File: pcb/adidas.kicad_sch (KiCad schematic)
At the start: 34 parts, among them J1 ISP Header, J7 Battery, J9 Shitty Add-on, U1 MPU-6050, U2 ATTINY841-SSU

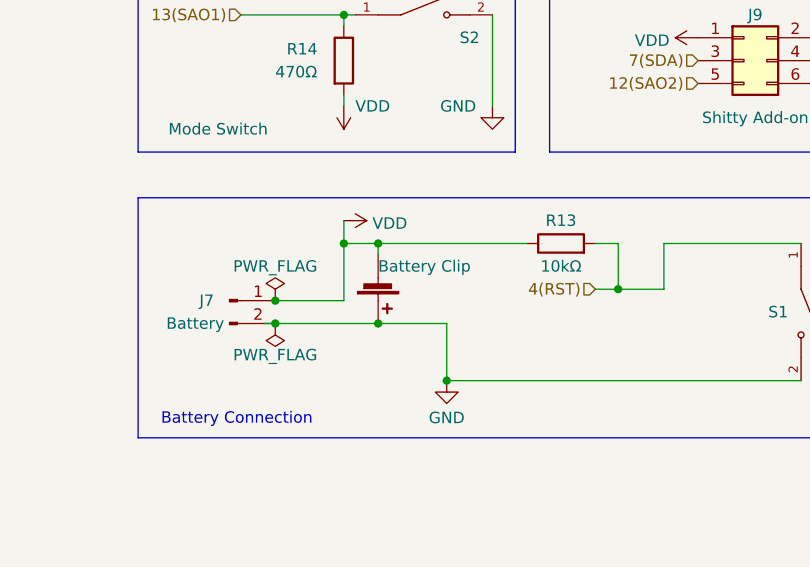
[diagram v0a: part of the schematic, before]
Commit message: fix reversed battery clip leads (#49)
* documentation updates

* documentation updates

* documentation updates

* fix battery clip
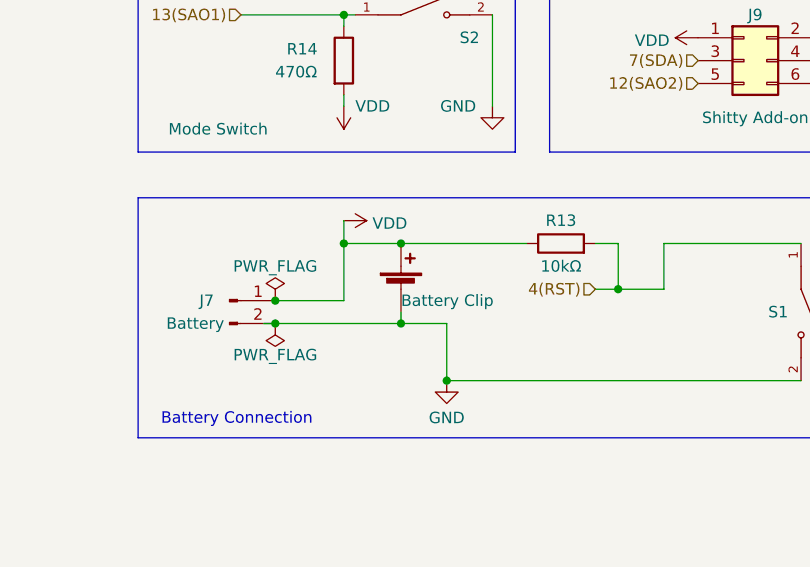
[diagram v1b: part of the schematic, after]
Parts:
- BT1: footprint Resistor_SMD:R_1206_3216Metric -> DEAD10C5:BatteryHolder_Keystone_3002_1x2032
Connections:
- net GND: now also BT1.2 (-); no longer BT1.1 (+)
- net VDD: now also BT1.1 (+); no longer BT1.2 (-)
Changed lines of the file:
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@@
     (comment 1 "Русский хардбасс")
   )
-  (junction (at 219.71 151.13) (diameter 0) (color 0 0 0 0)
-  )
   (junction (at 208.28 151.13) (diameter 0) (color 0 0 0 0)
   )
@@
   (junction (at 246.38 147.32) (diameter 0) (color 0 0 0 0)
   )
+  (junction (at 222.25 151.13) (diameter 0) (color 0 0 0 0)
+  )
   (junction (at 36.83 160.02) (diameter 0) (color 0 0 0 0)
   )
@@
   (junction (at 36.83 172.72) (diameter 0) (color 0 0 0 0)
   )
-  (junction (at 219.71 142.24) (diameter 0) (color 0 0 0 0)
-  )
   (junction (at 86.36 160.02) (diameter 0) (color 0 0 0 0)
   )
   (junction (at 111.76 160.02) (diameter 0) (color 0 0 0 0)
+  )
+  (junction (at 222.25 142.24) (diameter 0) (color 0 0 0 0)
   )
   (junction (at 168.91 160.02) (diameter 0) (color 0 0 0 0)
@@
     (stroke (width 0) (type default))
   )
-  (wire (pts (xy 219.71 151.13) (xy 227.33 151.13))
-    (stroke (width 0) (type default))
-  )
   (wire (pts (xy 215.9 116.84) (xy 217.17 116.84))
     (stroke (width 0) (type default))
   )
+  (wire (pts (xy 222.25 142.24) (xy 236.22 142.24))
+    (stroke (width 0) (type default))
+  )
   (wire (pts (xy 106.68 160.02) (xy 111.76 160.02))
     (stroke (width 0) (type default))
@@
     (stroke (width 0) (type default))
   )
-  (wire (pts (xy 219.71 142.24) (xy 236.22 142.24))
-    (stroke (width 0) (type default))
-  )
-  (wire (pts (xy 219.71 142.24) (xy 219.71 143.51))
+  (wire (pts (xy 215.9 142.24) (xy 222.25 142.24))
     (stroke (width 0) (type default))
   )
@@
     (stroke (width 0) (type default))
   )
+  (wire (pts (xy 222.25 151.13) (xy 227.33 151.13))
+    (stroke (width 0) (type default))
+  )
   (wire (pts (xy 224.79 50.8) (xy 224.79 53.34))
     (stroke (width 0) (type default))
@@
     (stroke (width 0) (type default))
   )
-  (wire (pts (xy 215.9 142.24) (xy 219.71 142.24))
-    (stroke (width 0) (type default))
-  )
   (wire (pts (xy 251.46 142.24) (xy 266.7 142.24))
     (stroke (width 0) (type default))
@@
     (stroke (width 0) (type default))
   )
-  (wire (pts (xy 208.28 151.13) (xy 219.71 151.13))
+  (wire (pts (xy 208.28 151.13) (xy 222.25 151.13))
+    (stroke (width 0) (type default))
+  )
+  (wire (pts (xy 222.25 149.86) (xy 222.25 151.13))
     (stroke (width 0) (type default))
   )
@@
     )
   )
-  (symbol (lib_id "Device:Battery_Cell") (at 219.71 146.05 0) (mirror x) (unit 1)
+  (symbol (lib_id "Device:Battery_Cell") (at 222.25 147.32 0) (unit 1)
     (in_bom no) (on_board yes) (dnp no)
-    (property "Reference" "BT1" (at 222.631 148.7257 0)
+    (property "Reference" "BT1" (at 225.171 144.6443 0)
       (effects (font (size 1.27 1.27)) (justify left) hide)
     )
-    (property "Value" "Battery Clip" (at 219.71 144.78 0)
-      (effects (font (size 1.27 1.27)) (justify left))
-    )
-    (property "Footprint" "Resistor_SMD:R_1206_3216Metric" (at 219.71 147.574 90)
-      (effects (font (size 1.27 1.27)) hide)
-    )
-    (property "Datasheet" "https://www.mouser.com/datasheet/2/215/3000TR-742873.pdf" (at 219.71 147.574 90)
-      (effects (font (size 1.27 1.27)) hide)
-    )
-    (property "Mouser Part Number`" "534-3000TR" (at 219.71 146.05 0)
-      (effects (font (size 1.27 1.27)) hide)
-    )
-    (property "Manufacturer Product Number" "3000TR" (at 219.71 146.05 0)
-      (effects (font (size 1.27 1.27)) hide)
-    )
-    (property "Manufacturer" "Keystone Electronics" (at 219.71 146.05 0)
-      (effects (font (size 1.27 1.27)) hide)
-    )
-    (property "Description" "CR2032 Coin Cell Battery Holder" (at 219.71 146.05 0)
-      (effects (font (size 1.27 1.27)) hide)
-    )
+    (property "Value" "Battery Clip" (at 222.25 148.59 0)
+      (effects (font (size 1.27 1.27)) (justify left))
+    )
+    (property "Footprint" "DEAD10C5:BatteryHolder_Keystone_3002_1x2032" (at 222.25 145.796 90)
+      (effects (font (size 1.27 1.27)) hide)
+    )
+    (property "Datasheet" "https://www.mouser.com/datasheet/2/215/3000TR-742873.pdf" (at 222.25 145.796 90)
+      (effects (font (size 1.27 1.27)) hide)
+    )
+    (property "Mouser Part Number`" "534-3000TR" (at 222.25 147.32 0)
+      (effects (font (size 1.27 1.27)) hide)
+    )
+    (property "Manufacturer Product Number" "3000TR" (at 222.25 147.32 0)
+      (effects (font (size 1.27 1.27)) hide)
+    )
+    (property "Manufacturer" "Keystone Electronics" (at 222.25 147.32 0)
+      (effects (font (size 1.27 1.27)) hide)
+    )
+    (property "Description" "CR2032 Coin Cell Battery Holder" (at 222.25 147.32 0)
+      (effects (font (size 1.27 1.27)) hide)
+    )

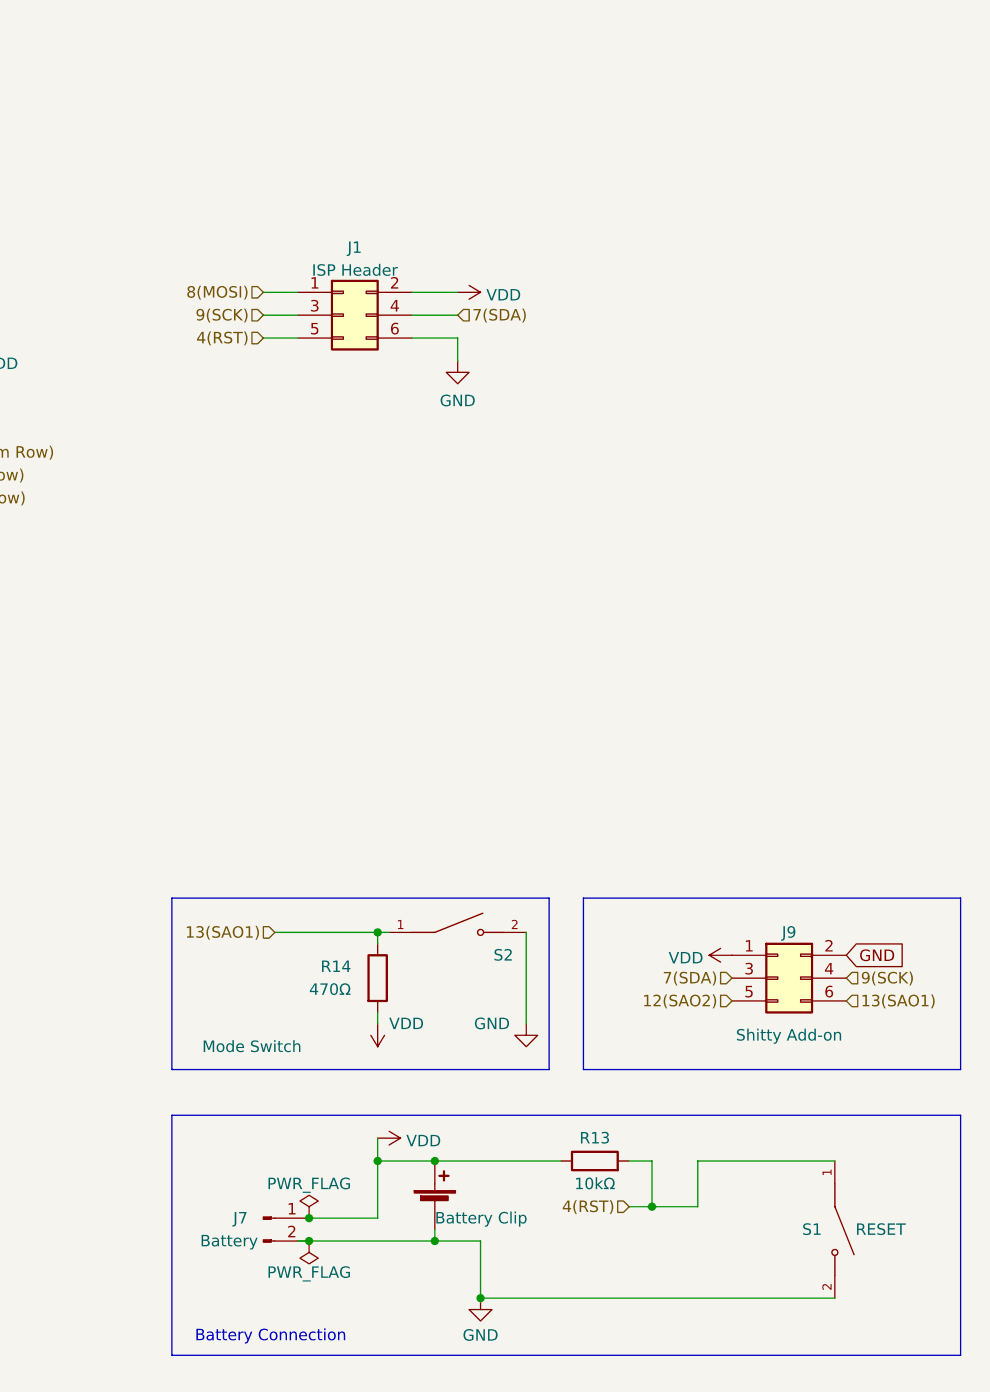
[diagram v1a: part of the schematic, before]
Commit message: hardware testing (#50)
* hardware testing

* hardware testing

* new hardware test with wire library

* add some docs on how the new test code is meant to work

* add docs for flashing the boards

* add test pin breakouts

* more testing

* checkpoint some test code

* add serial port

* testing pins

* testing pins
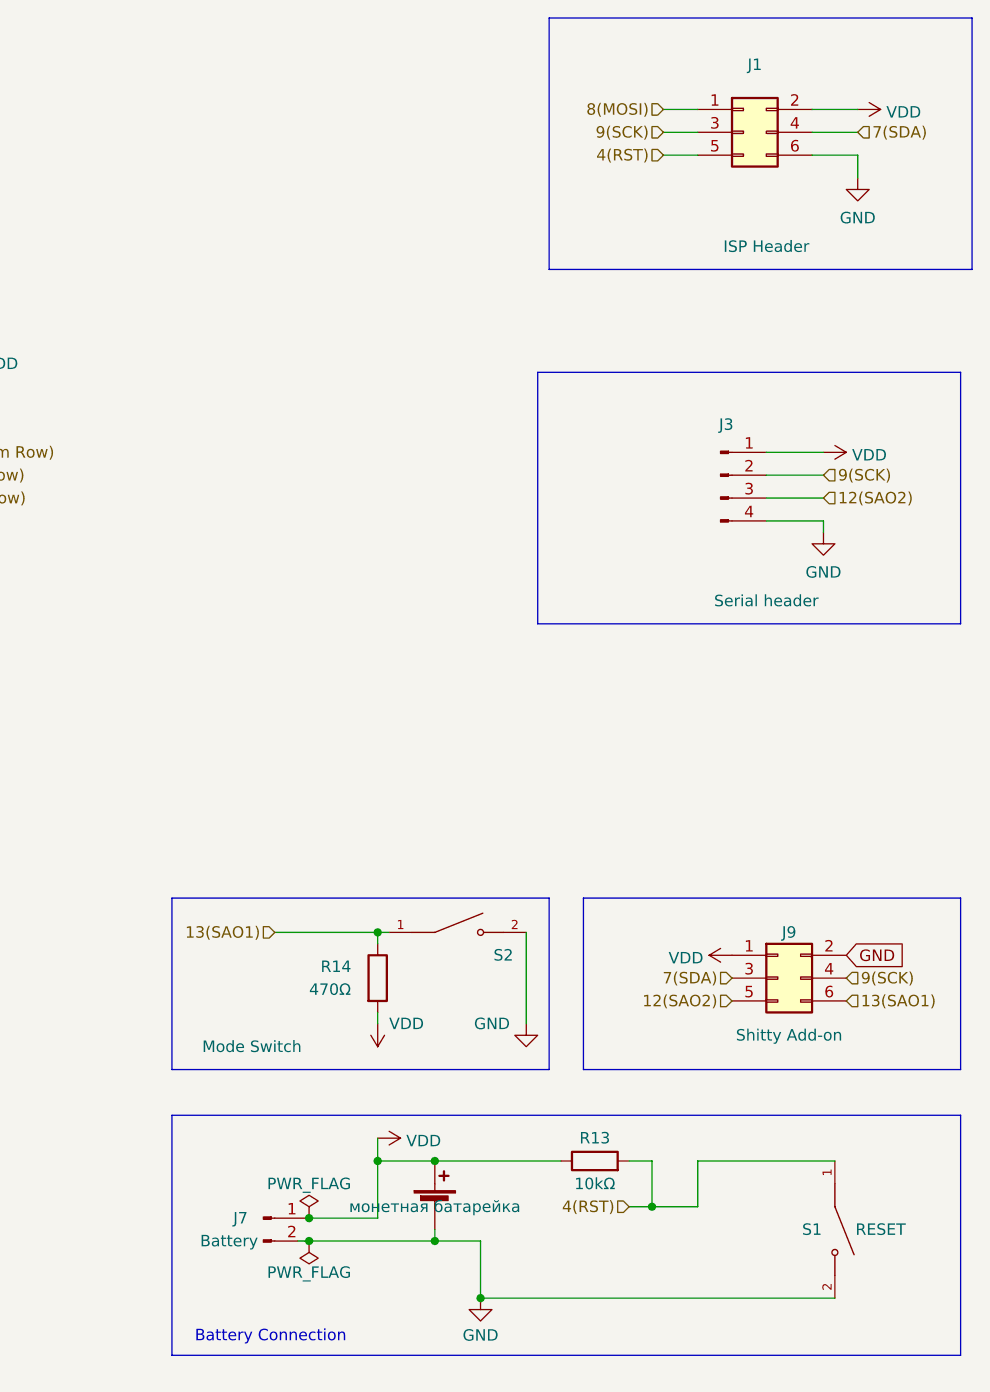
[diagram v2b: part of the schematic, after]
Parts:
- added J3: Conn_01x04_Pin, Connector_PinHeader_2.54mm:PinHeader_1x04_P2.54mm_Vertical, symbol Connector:Conn_01x04_Pin
- BT1: val (none) -> монетная батарейка
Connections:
- net 12(SAO2): now also J3.3 (Pin_3)
- net 9(SCK): now also J3.2 (Pin_2)
- net GND: now also J3.4 (Pin_4)
- net VDD: now also J3.1 (Pin_1)
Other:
- moved on the sheet: J1

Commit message: updates to the back of the board
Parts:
- BT1: value Battery Clip -> монетная батарейка
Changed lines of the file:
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@@
       (effects (font (size 1.27 1.27)) (justify left) hide)
     )
-    (property "Value" "Battery Clip" (at 222.25 148.59 0)
+    (property "Value" "монетная батарейка" (at 222.25 148.59 0)
       (effects (font (size 1.27 1.27)) (justify left) hide)
     )

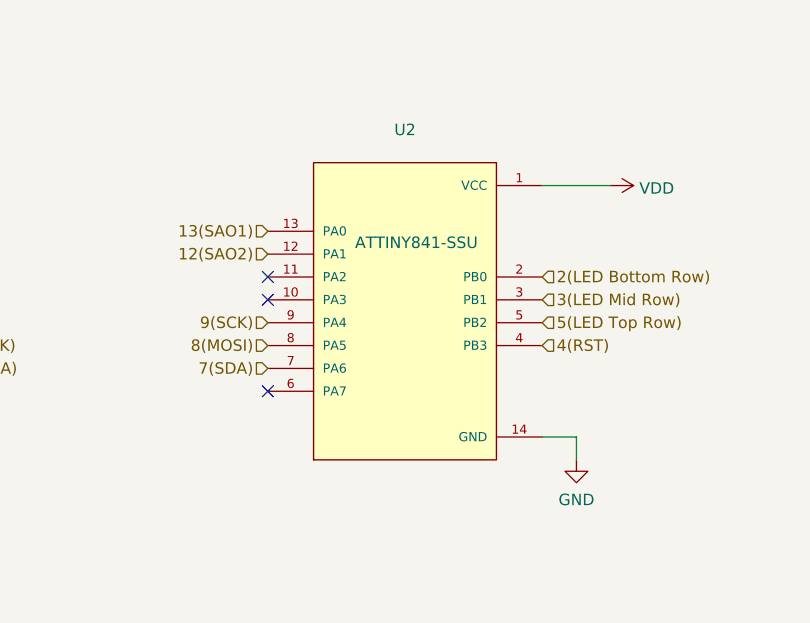
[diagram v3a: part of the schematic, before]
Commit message: flip the battery clip (#57)
* flip the battery clip

* update BOM and generate gerbers
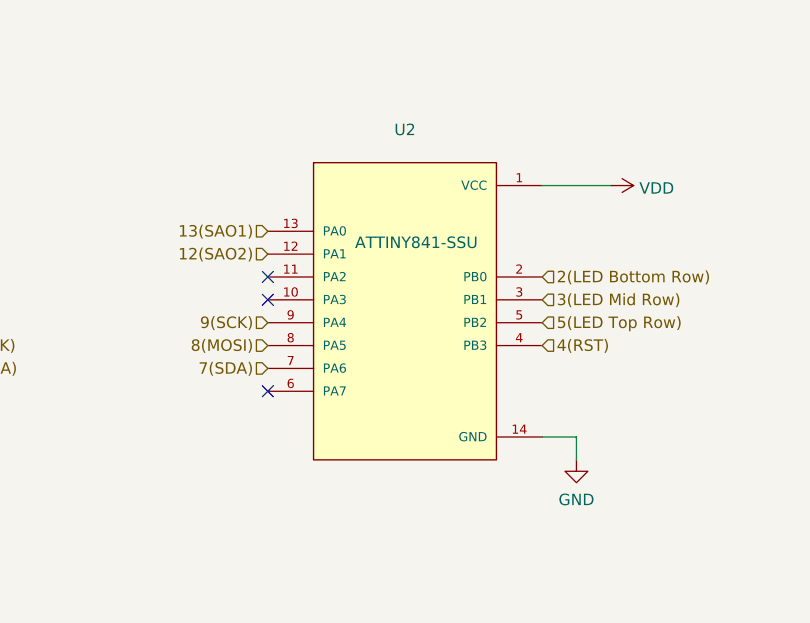
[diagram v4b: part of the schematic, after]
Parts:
- U2: A1_MIN 0.1 -> (none); A_MAX 1.75 -> (none); A_MIN 1.75 -> (none); A_NOM 1.75 -> (none); B_MAX 0.5 -> (none); B_MIN 0.33 -> (none); B_NOM 0.415 -> (none); D2_MAX 0.0 -> (none); D_MAX 8.74 -> (none); D_MIN 8.55 -> (none); D_NOM 8.645 -> (none); E1_MAX 3.99 -> (none); E1_MIN 3.8 -> (none); E1_NOM 3.895 -> (none); E2_MAX 0.0 -> (none); ENOM 1.27 -> (none); E_MAX 6.19 -> (none); E_MIN 5.8 -> (none); E_NOM 5.995 -> (none); L_MAX 1.27 -> (none); L_MIN 0.41 -> (none); L_NOM 0.84 -> (none); MANUFACTURER Microchip -> (none); MAXIMUM_PACKAGE_HEIGHT 1.75mm -> (none); Manufacturer Microchip -> (none); Mouser Part 556-ATTINY841-SSU -> (none); PACKAGE_TYPE SOIC-14 -> (none); PARTREV A -> (none); PIN_COUNT 14.0 -> (none); STANDARD IPC 7351B -> (none)
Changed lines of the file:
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@@
   (title_block
     (title "гопник badge")
-    (date "2023-05-11")
+    (date "2023-06-01")
     (rev "v0.3")
     (company "DE:AD:10:C5")
     (comment 1 "Русский хардбасс")
+    (comment 2 "DEFCON XXXI")
   )
   (junction (at 208.28 151.13) (diameter 0) (color 0 0 0 0)
@@
       (effects (font (size 1.27 1.27)) (justify left bottom) hide)
     )
-    (property "PACKAGE_TYPE" "SOIC-14" (at 146.05 66.04 0)
-      (effects (font (size 1.27 1.27)) (justify left bottom) hide)
-    )
-    (property "Manufacturer" "Microchip" (at 146.05 66.04 0)
-      (effects (font (size 1.27 1.27)) (justify left bottom) hide)
-    )
-    (property "MAXIMUM_PACKAGE_HEIGHT" "1.75mm" (at 146.05 66.04 0)
-      (effects (font (size 1.27 1.27)) (justify left bottom) hide)
-    )
-    (property "Mouser Part" "556-ATTINY841-SSU" (at 146.05 66.04 0)
-      (effects (font (size 1.27 1.27)) hide)
-    )
-    (property "B_NOM" "0.415" (at 146.05 66.04 0)
-      (effects (font (size 1.27 1.27)) (justify left bottom) hide)
-    )
-    (property "B_MIN" "0.33" (at 146.05 66.04 0)
-      (effects (font (size 1.27 1.27)) (justify left bottom) hide)
-    )
-    (property "D_MIN" "8.55" (at 146.05 66.04 0)
-      (effects (font (size 1.27 1.27)) (justify left bottom) hide)
-    )
-    (property "PINS" "" (at 146.05 66.04 0)
-      (effects (font (size 1.27 1.27)) (justify left bottom) hide)
-    )
-    (property "E2_MAX" "0.0" (at 146.05 66.04 0)
-      (effects (font (size 1.27 1.27)) (justify left bottom) hide)
-    )
-    (property "L1_MIN" "" (at 146.05 66.04 0)
-      (effects (font (size 1.27 1.27)) (justify left bottom) hide)
-    )
-    (property "D1_NOM" "" (at 146.05 66.04 0)
-      (effects (font (size 1.27 1.27)) (justify left bottom) hide)
-    )
-    (property "PARTREV" "A" (at 146.05 66.04 0)
-      (effects (font (size 1.27 1.27)) (justify left bottom) hide)
-    )
-    (property "A_NOM" "1.75" (at 146.05 66.04 0)
-      (effects (font (size 1.27 1.27)) (justify left bottom) hide)
-    )
-    (property "STANDARD" "IPC 7351B" (at 146.05 66.04 0)
-      (effects (font (size 1.27 1.27)) (justify left bottom) hide)
-    )
-    (property "D1_MIN" "" (at 146.05 66.04 0)
-      (effects (font (size 1.27 1.27)) (justify left bottom) hide)
-    )
-    (property "D_MAX" "8.74" (at 146.05 66.04 0)
-      (effects (font (size 1.27 1.27)) (justify left bottom) hide)
-    )
-    (property "L1_MAX" "" (at 146.05 66.04 0)
-      (effects (font (size 1.27 1.27)) (justify left bottom) hide)
-    )
-    (property "VACANCIES" "" (at 146.05 66.04 0)
-      (effects (font (size 1.27 1.27)) (justify left bottom) hide)
-    )
-    (property "E1_MAX" "3.99" (at 146.05 66.04 0)
-      (effects (font (size 1.27 1.27)) (justify left bottom) hide)
-    )
-    (property "DMIN" "" (at 146.05 66.04 0)
-      (effects (font (size 1.27 1.27)) (justify left bottom) hide)
-    )
-    (property "E1_MIN" "3.8" (at 146.05 66.04 0)
-      (effects (font (size 1.27 1.27)) (justify left bottom) hide)
-    )
-    (property "MANUFACTURER" "Microchip" (at 146.05 66.04 0)
-      (effects (font (size 1.27 1.27)) (justify left bottom) hide)
-    )
-    (property "L_MAX" "1.27" (at 146.05 66.04 0)
-      (effects (font (size 1.27 1.27)) (justify left bottom) hide)
-    )
-    (property "E1_NOM" "3.895" (at 146.05 66.04 0)
-      (effects (font (size 1.27 1.27)) (justify left bottom) hide)
-    )
-    (property "E_MAX" "6.19" (at 146.05 66.04 0)
-      (effects (font (size 1.27 1.27)) (justify left bottom) hide)
-    )
-    (property "D1_MAX" "" (at 146.05 66.04 0)
-      (effects (font (size 1.27 1.27)) (justify left bottom) hide)
-    )
-    (property "DMAX" "" (at 146.05 66.04 0)
-      (effects (font (size 1.27 1.27)) (justify left bottom) hide)
-    )
-    (property "E_NOM" "5.995" (at 146.05 66.04 0)
-      (effects (font (size 1.27 1.27)) (justify left bottom) hide)
-    )
-    (property "D_NOM" "8.645" (at 146.05 66.04 0)
-      (effects (font (size 1.27 1.27)) (justify left bottom) hide)
-    )
-    (property "A_MIN" "1.75" (at 146.05 66.04 0)
-      (effects (font (size 1.27 1.27)) (justify left bottom) hide)
-    )
-    (property "B_MAX" "0.5" (at 146.05 66.04 0)
-      (effects (font (size 1.27 1.27)) (justify left bottom) hide)
-    )
-    (property "ENOM" "1.27" (at 146.05 66.04 0)
-      (effects (font (size 1.27 1.27)) (justify left bottom) hide)
-    )
-    (property "D2_MAX" "0.0" (at 146.05 66.04 0)
-      (effects (font (size 1.27 1.27)) (justify left bottom) hide)
-    )
-    (property "SNAPEDA_PACKAGE_ID" "" (at 146.05 66.04 0)
-      (effects (font (size 1.27 1.27)) (justify left bottom) hide)
-    )
-    (property "L_NOM" "0.84" (at 146.05 66.04 0)
-      (effects (font (size 1.27 1.27)) (justify left bottom) hide)
-    )
-    (property "DNOM" "" (at 146.05 66.04 0)
-      (effects (font (size 1.27 1.27)) (justify left bottom) hide)
-    )
-    (property "EMIN" "" (at 146.05 66.04 0)
-      (effects (font (size 1.27 1.27)) (justify left bottom) hide)
-    )
-    (property "A_MAX" "1.75" (at 146.05 66.04 0)
-      (effects (font (size 1.27 1.27)) (justify left bottom) hide)
-    )
-    (property "PIN_COUNT" "14.0" (at 146.05 66.04 0)
-      (effects (font (size 1.27 1.27)) (justify left bottom) hide)
-    )
-    (property "EMAX" "" (at 146.05 66.04 0)
-      (effects (font (size 1.27 1.27)) (justify left bottom) hide)
-    )
-    (property "A1_MIN" "0.1" (at 146.05 66.04 0)
-      (effects (font (size 1.27 1.27)) (justify left bottom) hide)
-    )
-    (property "E_MIN" "5.8" (at 146.05 66.04 0)
-      (effects (font (size 1.27 1.27)) (justify left bottom) hide)
-    )
-    (property "L1_NOM" "" (at 146.05 66.04 0)
-      (effects (font (size 1.27 1.27)) (justify left bottom) hide)
-    )
-    (property "L_MIN" "0.41" (at 146.05 66.04 0)
-      (effects (font (size 1.27 1.27)) (justify left bottom) hide)
-    )
